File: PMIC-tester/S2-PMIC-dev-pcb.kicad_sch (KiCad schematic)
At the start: 17 parts, among them J1 USB_C_Receptacle_USB2.0, P1 CONN_02X13, P3 CONN_02X13, SW1 RESET, SW2 BOOT, U1 MCP1700-1202E_SOT23, U2 ESP32-S2-WROVER, U3 TPS65185RGZR

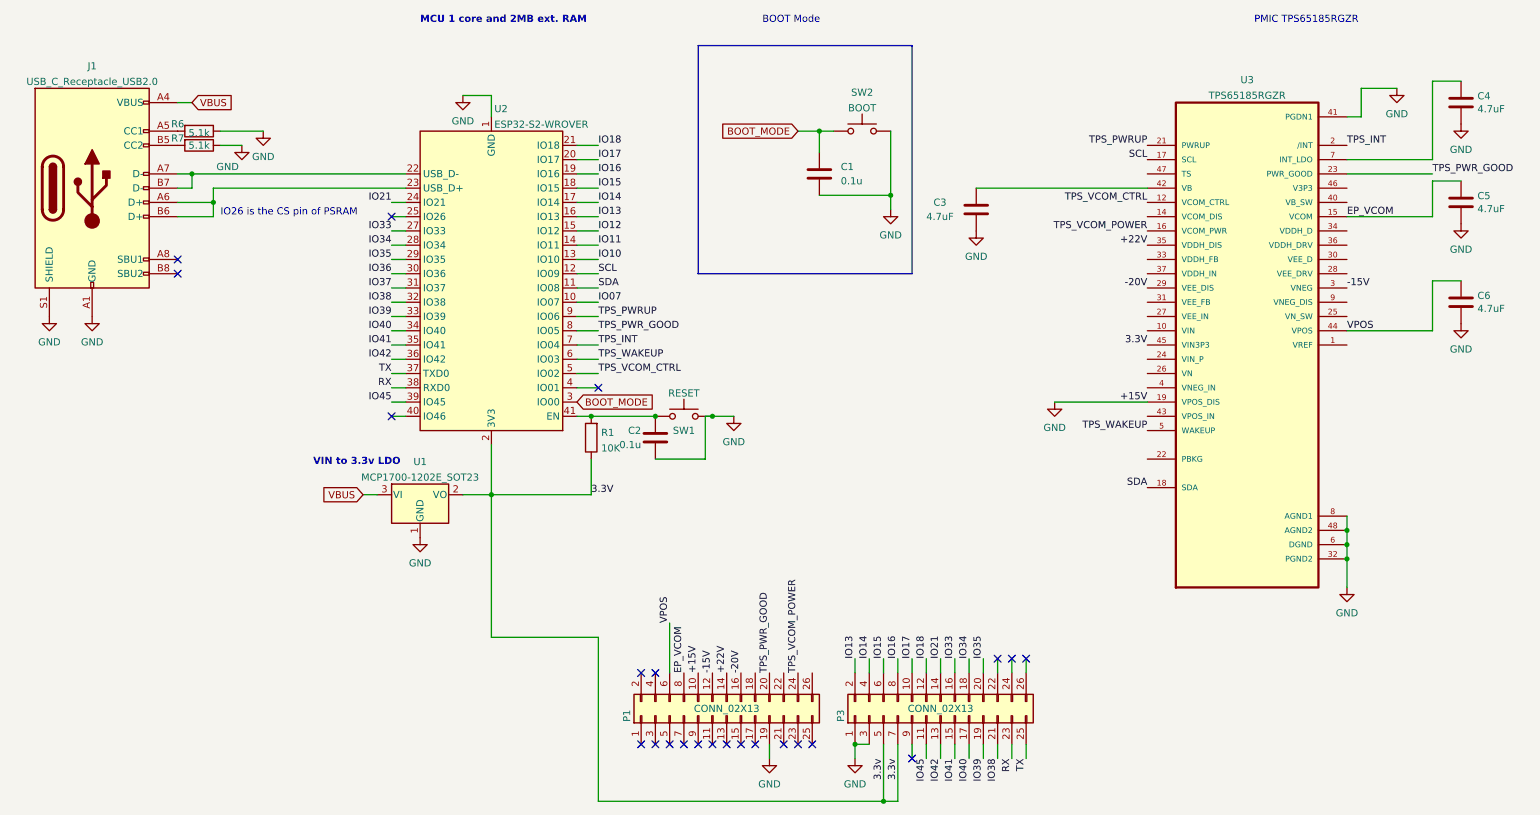
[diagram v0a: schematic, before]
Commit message: Minimal update with TPs
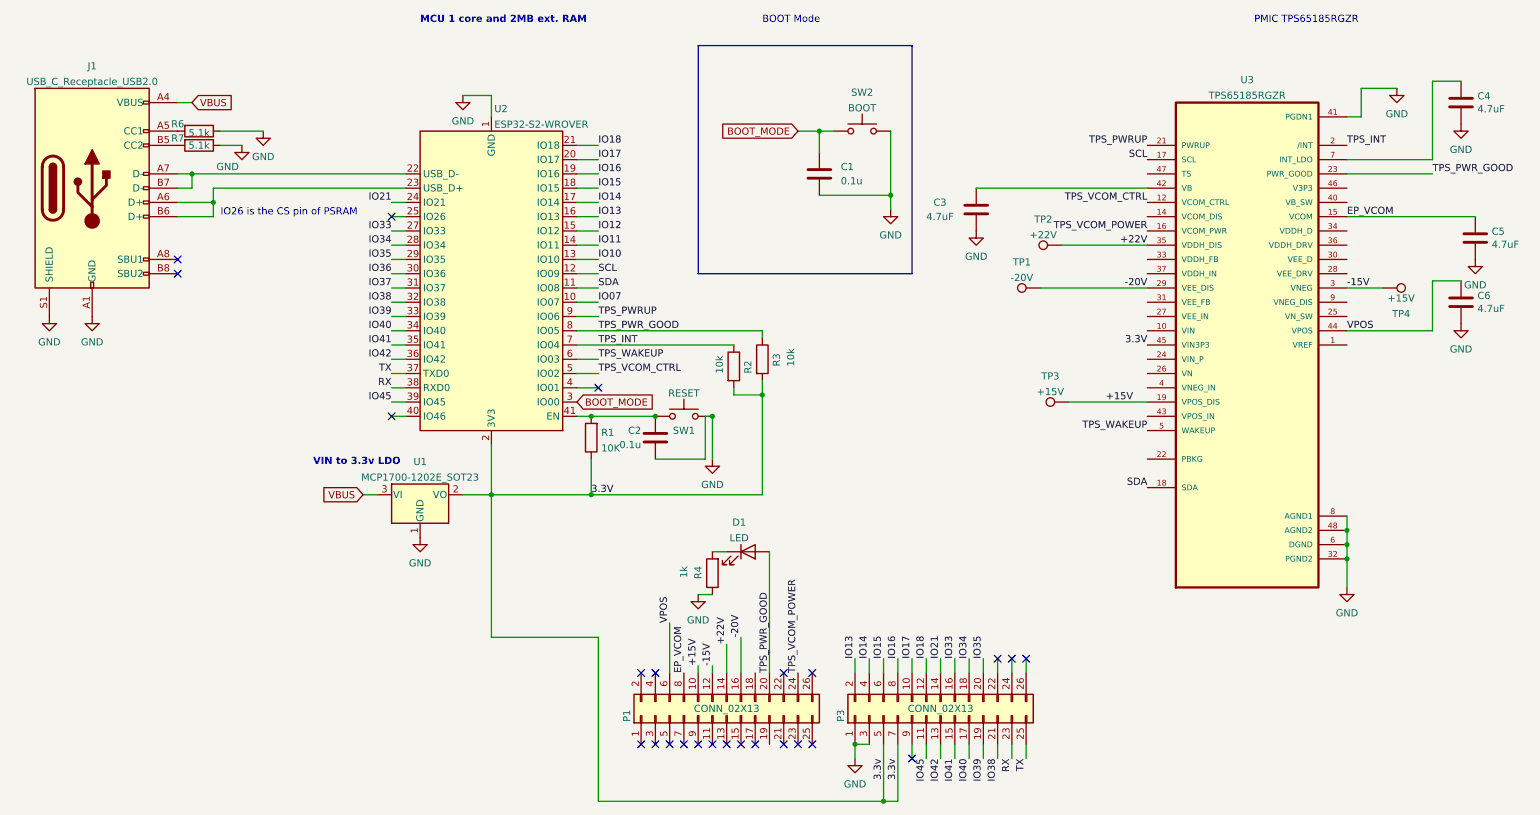
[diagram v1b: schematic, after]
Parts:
- added D1: LED, LED_THT:LED_D1.8mm_W3.3mm_H2.4mm, symbol Device:LED
- added R2, R3: 10k, Resistor_SMD:R_0603_1608Metric, symbol Device:R
- added R4: 1k, Resistor_SMD:R_0603_1608Metric, symbol Device:R
- added TP1: -20V, TestPoint:TestPoint_Pad_D2.0mm, symbol Connector:TestPoint
- added TP2: +22V, TestPoint:TestPoint_Pad_D2.0mm, symbol Connector:TestPoint
- added TP3, TP4: +15V, TestPoint:TestPoint_Pad_D2.0mm, symbol Connector:TestPoint
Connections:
- net +22V: now also TP2.1
- net -15V: now also TP4.1
- net -20V: now also TP1.1
- net 3.3V: now also R2.2, R3.2
- net GND: now also R4.1; no longer P1.10 (Pin_10), P1.19 (Pin_19), U3.19 (VPOS_DIS)
- net TPS_INT: now also R2.1
- net TPS_PWR_GOOD: now also D1.2 (A), R3.1
- new net: D1.1 (K), R4.2
- new net +15V: P1.10 (Pin_10), TP3.1, U3.19 (VPOS_DIS)
- no-connect marks 23 -> 25
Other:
- moved on the sheet: C5
